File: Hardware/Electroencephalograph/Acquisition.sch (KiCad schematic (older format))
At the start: 68 parts, among them J8 Conn_01x02_Male, U1 ADS1298IPAG, U2 OPA330xxD

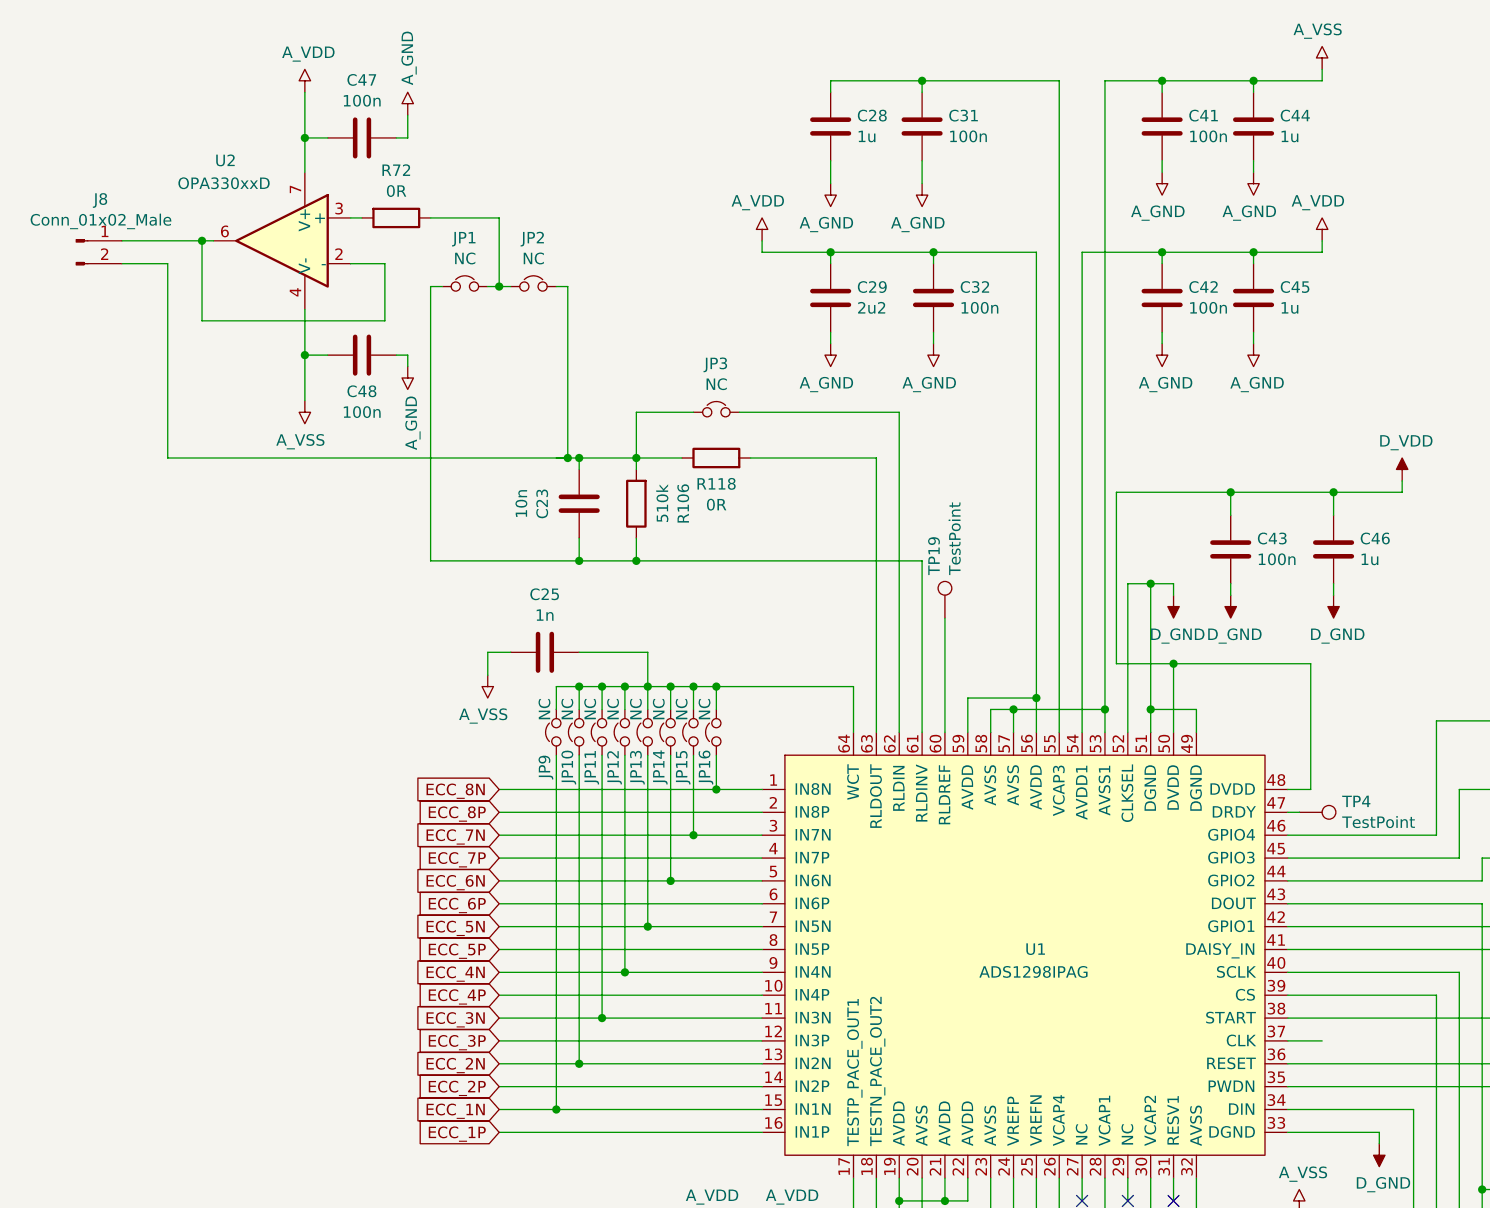
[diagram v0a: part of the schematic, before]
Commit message: add bom
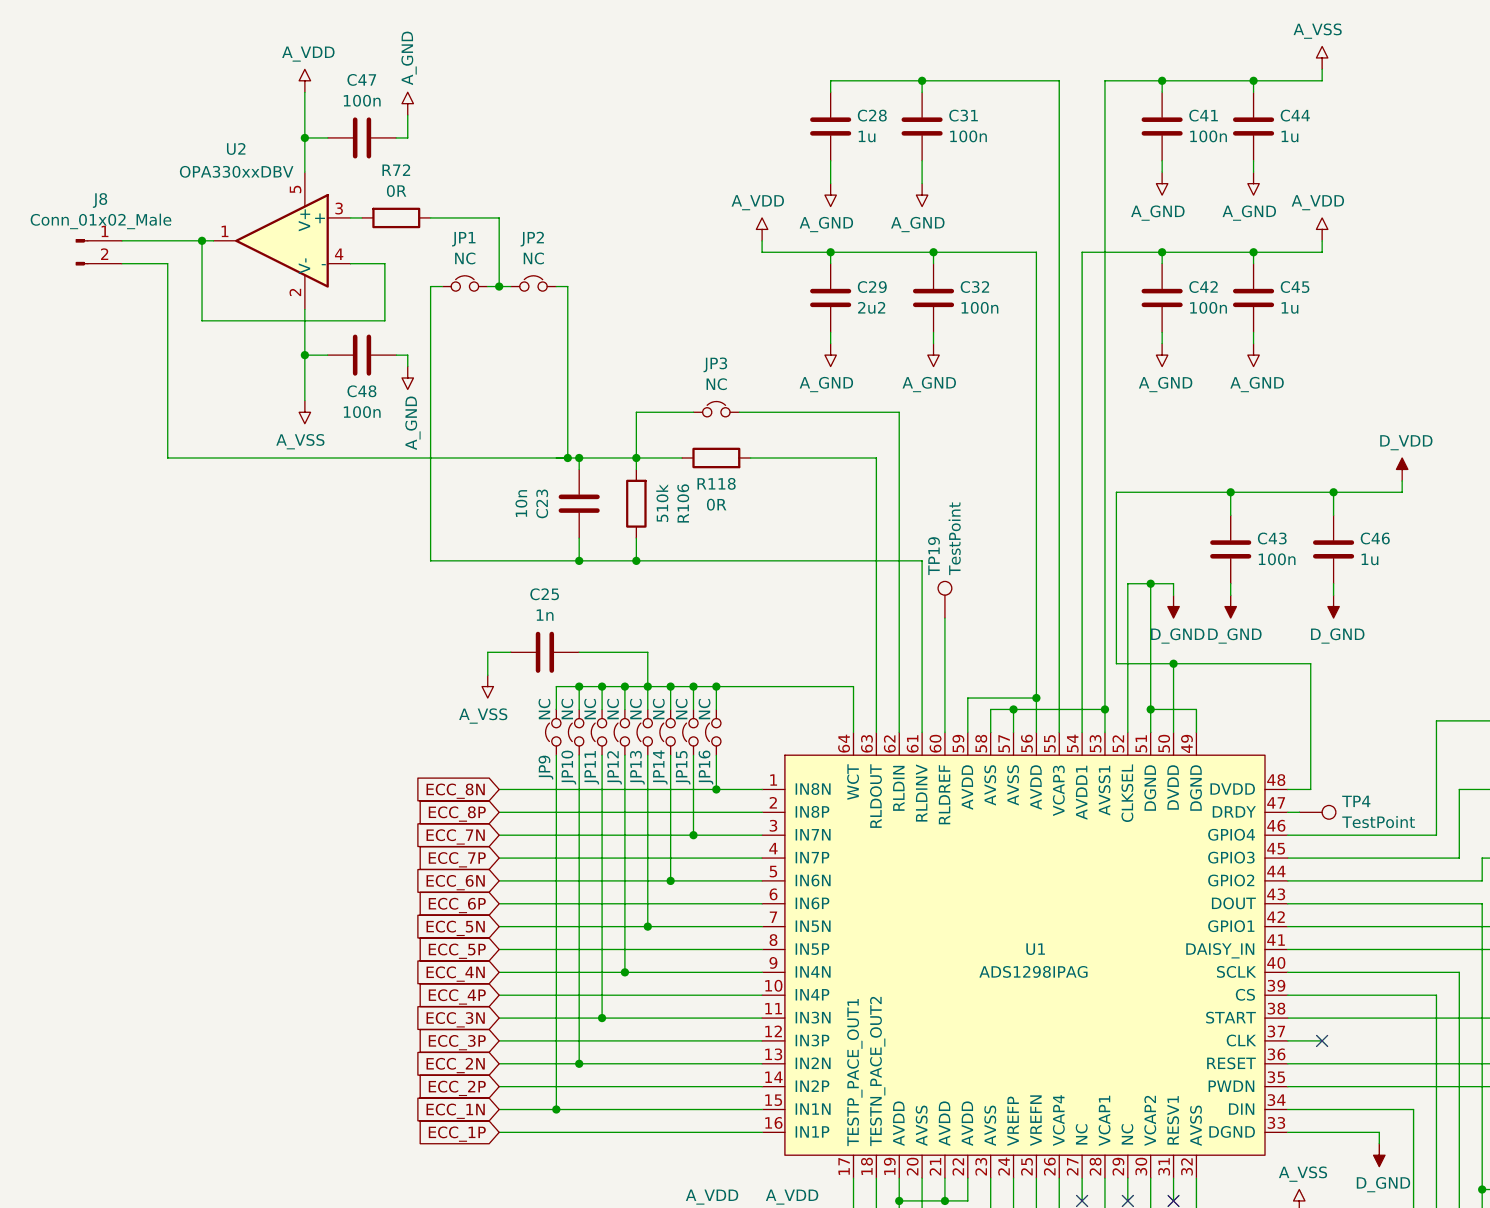
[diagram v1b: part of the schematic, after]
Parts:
- removed U2: OPA330xxD, Package_SO:SOIC-8_3.9x4.9mm_P1.27mm, symbol Amplifier_Operational:OPA330xxD
- added U2: OPA330xxDBV, Package_TO_SOT_SMD:SOT-23-5, symbol Amplifier_Operational:OPA330xxDBV
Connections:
- net A_VDD: now also U2.5 (V+)
- net A_VSS: now also U2.2 (V-)
- net at J8.1 (Pin_1): now also U2.1, U2.4 (-)
- net at R72.2: now also U2.3 (+)
- no-connect marks 3 -> 4
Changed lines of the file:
@@
 	5200 6500 5200 6450
-$Comp
-L Amplifier_Operational:OPA330xxD U2
-U 1 1 5DF9ACC1
-P 1600 1450
-F 0 "U2" H 1800 1800 50  0000 L CNN
-F 1 "OPA330xxD" H 1650 1700 50  0000 L CNN
-F 2 "Package_SO:SOIC-8_3.9x4.9mm_P1.27mm" H 1500 1250 50  0001 L CNN
-F 3 "http://www.ti.com/lit/ds/symlink/opa330.pdf" H 1750 1600 50  0001 C CNN
-	1    1600 1450
-	-1   0    0    -1
-$EndComp
 $Comp
 L Device:C C?
@@
 	1    0    0    -1
 $EndComp
+$Comp
+L Amplifier_Operational:OPA330xxDBV U2
+U 1 1 60DAF198
+P 1600 1450
+F 0 "U2" H 1800 1850 50  0000 C CNN
+F 1 "OPA330xxDBV" H 1800 1750 50  0000 C CNN
+F 2 "Package_TO_SOT_SMD:SOT-23-5" H 1500 1250 50  0001 L CNN
+F 3 "http://www.ti.com/lit/ds/symlink/opa330.pdf" H 1600 1650 50  0001 C CNN
+	1    1600 1450
+	-1   0    0    -1
+$EndComp
+NoConn ~ 6150 4950
 $EndSCHEMATC
